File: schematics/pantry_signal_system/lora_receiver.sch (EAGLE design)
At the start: 6 parts, among them J1 JST-XH254-2P, U1 ESP32, U12 E220-900T22D, U2 SN74LVC2T45DCUR, U3 SN74LVC2T45DCUR

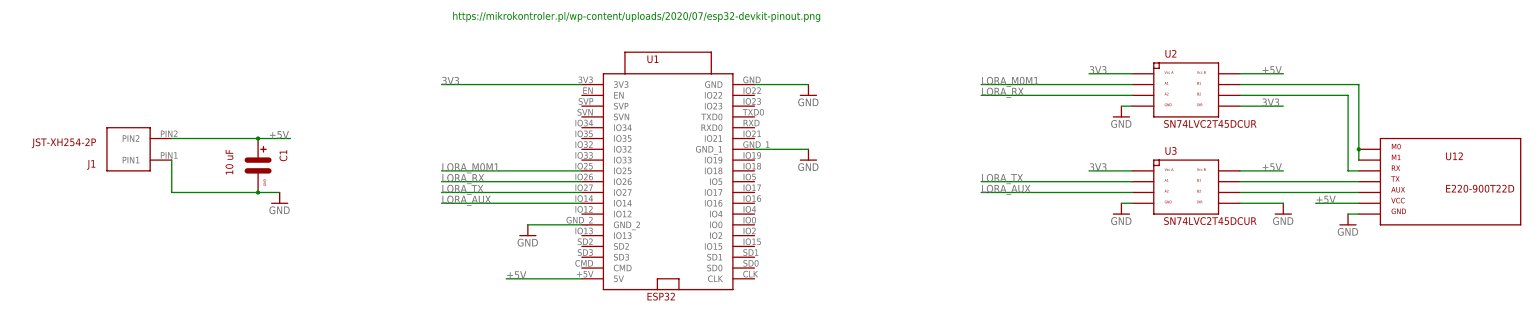
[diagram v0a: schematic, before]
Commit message: Changes in schematics, changes in source code. Current version works too, but I changed boards to fix some possible errors
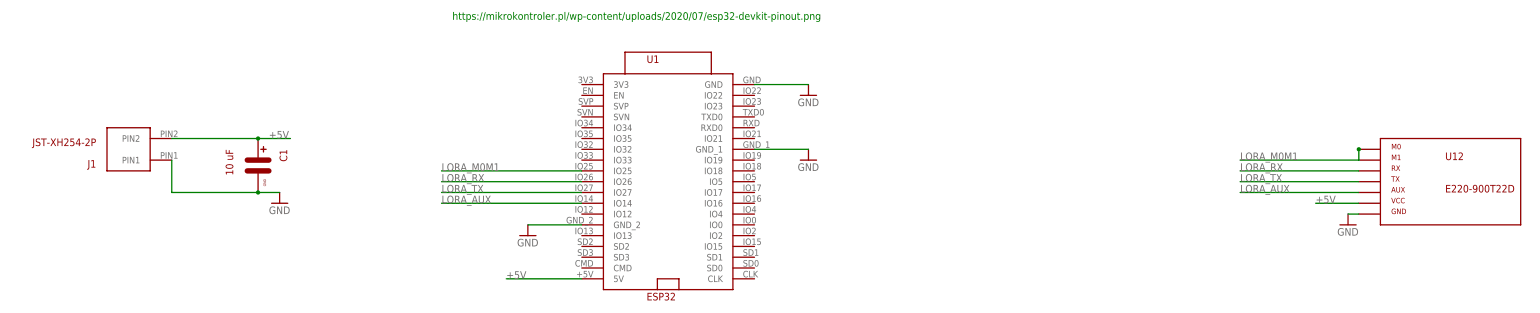
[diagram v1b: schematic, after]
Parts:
- removed U2, U3: SN74LVC2T45DCUR, my_devices:LEVEL_CONVERTER_2L
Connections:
- removed net 3V3: U1.3V3, U2.DIR, U2.VCCA, U3.VCCA
- removed net N$1: U12.TX, U3.B1
- removed net N$2: U12.RX, U2.B2
- removed net N$3: U12.AUX, U3.B2
- removed net N$9: U12.M0, U12.M1, U2.B1
- net +5V: no longer U2.VCCB, U3.VCCB
- net GND: no longer U2.GND, U3.DIR, U3.GND
- net LORA_AUX: now also U12.AUX; no longer U3.A2
- net LORA_M0M1: now also U12.M0, U12.M1; no longer U2.A1
- net LORA_RX: now also U12.RX; no longer U2.A2
- net LORA_TX: now also U12.TX; no longer U3.A1
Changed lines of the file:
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@@
 <part name="J1" library="my_devices" deviceset="JST-XH254-2P" device=""/>
 <part name="GND4" library="supply1" library_urn="urn:adsk.eagle:library:371" deviceset="GND" device=""/>
-<part name="U2" library="my_devices" deviceset="LEVEL_CONVERTER_2L" device="" value="SN74LVC2T45DCUR"/>
-<part name="U3" library="my_devices" deviceset="LEVEL_CONVERTER_2L" device="" value="SN74LVC2T45DCUR"/>
-<part name="GND5" library="supply1" library_urn="urn:adsk.eagle:library:371" deviceset="GND" device=""/>
-<part name="GND6" library="supply1" library_urn="urn:adsk.eagle:library:371" deviceset="GND" device=""/>
-<part name="GND7" library="supply1" library_urn="urn:adsk.eagle:library:371" deviceset="GND" device=""/>
 <part name="GND8" library="supply1" library_urn="urn:adsk.eagle:library:371" deviceset="GND" device=""/>
 <part name="C1" library="my_devices" deviceset="C" device="MINI-5X7" value="10 uF"/>
@@
 <attribute name="VALUE" x="-71.12" y="119.38" size="1.778" layer="96"/>
 </instance>
-<instance part="U2" gate="G$1" x="144.78" y="147.32" smashed="yes" grouprefs="LORA">
-<attribute name="NAME" x="139.7" y="156.21" size="1.778" layer="94"/>
-<attribute name="VALUE" x="139.446" y="139.7" size="1.778" layer="94"/>
-</instance>
-<instance part="U3" gate="G$1" x="144.78" y="124.46" smashed="yes" grouprefs="LORA">
-<attribute name="NAME" x="139.7" y="133.35" size="1.778" layer="94"/>
-<attribute name="VALUE" x="139.446" y="116.84" size="1.778" layer="94"/>
-</instance>
-<instance part="GND5" gate="1" x="129.54" y="142.24" smashed="yes" grouprefs="LORA">
-<attribute name="VALUE" x="127" y="139.7" size="1.778" layer="96"/>
-</instance>
-<instance part="GND6" gate="1" x="129.54" y="119.38" smashed="yes" grouprefs="LORA">
-<attribute name="VALUE" x="127" y="116.84" size="1.778" layer="96"/>
-</instance>
-<instance part="GND7" gate="1" x="167.64" y="119.38" smashed="yes" grouprefs="LORA">
-<attribute name="VALUE" x="165.1" y="116.84" size="1.778" layer="96"/>
-</instance>
 <instance part="GND8" gate="1" x="182.88" y="116.84" smashed="yes" grouprefs="LORA">
 <attribute name="VALUE" x="180.34" y="114.3" size="1.778" layer="96"/>
@@
 <pinref part="GND2" gate="1" pin="GND"/>
 <wire x1="43.18" y1="149.86" x2="55.88" y2="149.86" width="0.1524" layer="91" grouprefs="ESP32"/>
-</segment>
-<segment>
-<pinref part="GND5" gate="1" pin="GND"/>
-<pinref part="U2" gate="G$1" pin="GND"/>
-<wire x1="129.54" y1="144.78" x2="132.08" y2="144.78" width="0.1524" layer="91" grouprefs="LORA"/>
-</segment>
-<segment>
-<pinref part="GND6" gate="1" pin="GND"/>
-<pinref part="U3" gate="G$1" pin="GND"/>
-<wire x1="129.54" y1="121.92" x2="132.08" y2="121.92" width="0.1524" layer="91" grouprefs="LORA"/>
-</segment>
-<segment>
-<pinref part="U3" gate="G$1" pin="DIR"/>
-<pinref part="GND7" gate="1" pin="GND"/>
-<wire x1="157.48" y1="121.92" x2="167.64" y2="121.92" width="0.1524" layer="91" grouprefs="LORA"/>
 </segment>
 <segment>
@@
 </segment>
 <segment>
-<pinref part="U2" gate="G$1" pin="VCCB"/>
-<wire x1="157.48" y1="152.4" x2="167.64" y2="152.4" width="0.1524" layer="91" grouprefs="LORA"/>
-<label x="162.56" y="152.4" size="1.778" layer="95" grouprefs="LORA"/>
-</segment>
-<segment>
-<pinref part="U3" gate="G$1" pin="VCCB"/>
-<wire x1="157.48" y1="129.54" x2="167.64" y2="129.54" width="0.1524" layer="91" grouprefs="LORA"/>
-<label x="162.56" y="129.54" size="1.778" layer="95" grouprefs="LORA"/>
-</segment>
-<segment>
 <pinref part="U12" gate="G$1" pin="VCC"/>
 <wire x1="185.42" y1="121.92" x2="175.26" y2="121.92" width="0.1524" layer="91" grouprefs="LORA"/>
@@
 <net name="LORA_RX" class="0">
 <segment>
-<pinref part="U2" gate="G$1" pin="A2"/>
-<wire x1="132.08" y1="147.32" x2="96.52" y2="147.32" width="0.1524" layer="91" grouprefs="LORA"/>
-<label x="96.52" y="147.32" size="1.778" layer="95" grouprefs="LORA"/>
-</segment>
-<segment>
 <pinref part="U1" gate="G$1" pin="IO26"/>
 <wire x1="2.54" y1="127" x2="-30.48" y2="127" width="0.1524" layer="91" grouprefs="ESP32"/>
 <label x="-30.48" y="127" size="1.778" layer="95" grouprefs="ESP32"/>
 </segment>
+<segment>
+<pinref part="U12" gate="G$1" pin="RX"/>
+<wire x1="185.42" y1="129.54" x2="157.48" y2="129.54" width="0.1524" layer="91" grouprefs="LORA"/>
+<label x="157.48" y="129.54" size="1.778" layer="95"/>
+</segment>
 </net>
 <net name="LORA_TX" class="0">
-<segment>
-<pinref part="U3" gate="G$1" pin="A1"/>
-<wire x1="132.08" y1="127" x2="96.52" y2="127" width="0.1524" layer="91" grouprefs="LORA"/>
-<label x="96.52" y="127" size="1.778" layer="95" grouprefs="LORA"/>
-</segment>
 <segment>
 <pinref part="U1" gate="G$1" pin="IO27"/>
@@
 <label x="-30.48" y="124.46" size="1.778" layer="95" grouprefs="ESP32"/>
 </segment>
+<segment>
+<pinref part="U12" gate="G$1" pin="TX"/>
+<wire x1="157.48" y1="127" x2="185.42" y2="127" width="0.1524" layer="91" grouprefs="LORA"/>
+<label x="157.48" y="127" size="1.778" layer="95"/>
+</segment>
 </net>
 <net name="LORA_AUX" class="0">
-<segment>
-<pinref part="U3" gate="G$1" pin="A2"/>
-<wire x1="132.08" y1="124.46" x2="96.52" y2="124.46" width="0.1524" layer="91" grouprefs="LORA"/>
-<label x="96.52" y="124.46" size="1.778" layer="95" grouprefs="LORA"/>
-</segment>
 <segment>
 <pinref part="U1" gate="G$1" pin="IO14"/>
 <wire x1="2.54" y1="121.92" x2="-30.48" y2="121.92" width="0.1524" layer="91" grouprefs="ESP32"/>
 <label x="-30.48" y="121.92" size="1.778" layer="95" grouprefs="ESP32"/>
+</segment>
+<segment>
+<pinref part="U12" gate="G$1" pin="AUX"/>
+<wire x1="157.48" y1="124.46" x2="185.42" y2="124.46" width="0.1524" layer="91" grouprefs="LORA"/>
+<label x="157.48" y="124.46" size="1.778" layer="95"/>
 </segment>
 </net>
@@
 </segment>
 <segment>
-<pinref part="U2" gate="G$1" pin="A1"/>
-<wire x1="132.08" y1="149.86" x2="96.52" y2="149.86" width="0.1524" layer="91" grouprefs="LORA"/>
-<label x="96.52" y="149.86" size="1.778" layer="95" grouprefs="LORA"/>
+<pinref part="U12" gate="G$1" pin="M1"/>
+<pinref part="U12" gate="G$1" pin="M0"/>
+<wire x1="157.48" y1="132.08" x2="185.42" y2="132.08" width="0.1524" layer="91" grouprefs="LORA"/>
+<wire x1="185.42" y1="132.08" x2="185.42" y2="134.62" width="0.1524" layer="91" grouprefs="LORA"/>
+<junction x="185.42" y="134.62" grouprefs="LORA"/>
+<label x="157.48" y="132.08" size="1.778" layer="95"/>
 </segment>
 </net>
-<net name="N$9" class="0">
-<segment>
-<pinref part="U12" gate="G$1" pin="M1"/>
-<pinref part="U12" gate="G$1" pin="M0"/>
-<wire x1="185.42" y1="132.08" x2="185.42" y2="134.62" width="0.1524" layer="91" grouprefs="LORA"/>
-<pinref part="U2" gate="G$1" pin="B1"/>
-<wire x1="157.48" y1="149.86" x2="185.42" y2="149.86" width="0.1524" layer="91" grouprefs="LORA"/>
-<wire x1="185.42" y1="149.86" x2="185.42" y2="134.62" width="0.1524" layer="91" grouprefs="LORA"/>
-<junction x="185.42" y="134.62" grouprefs="LORA"/>
-</segment>
-</net>
-<net name="3V3" class="0">
-<segment>
-<pinref part="U1" gate="G$1" pin="3V3"/>
-<wire x1="2.54" y1="149.86" x2="-30.48" y2="149.86" width="0.1524" layer="91"/>
-<label x="-30.48" y="149.86" size="1.778" layer="95"/>
-</segment>
-<segment>
-<pinref part="U2" gate="G$1" pin="VCCA"/>
-<wire x1="132.08" y1="152.4" x2="121.92" y2="152.4" width="0.1524" layer="91" grouprefs="LORA"/>
-<label x="121.92" y="152.4" size="1.778" layer="95" grouprefs="LORA"/>
-</segment>
-<segment>
-<pinref part="U3" gate="G$1" pin="VCCA"/>
-<wire x1="132.08" y1="129.54" x2="121.92" y2="129.54" width="0.1524" layer="91" grouprefs="LORA"/>
-<label x="121.92" y="129.54" size="1.778" layer="95" grouprefs="LORA"/>
-</segment>
-<segment>
-<pinref part="U2" gate="G$1" pin="DIR"/>
-<wire x1="157.48" y1="144.78" x2="167.64" y2="144.78" width="0.1524" layer="91" grouprefs="LORA"/>
-<label x="162.56" y="144.78" size="1.778" layer="95" grouprefs="LORA"/>
-</segment>
-</net>
-<net name="N$2" class="0">
-<segment>
-<pinref part="U12" gate="G$1" pin="RX"/>
-<wire x1="185.42" y1="129.54" x2="182.88" y2="129.54" width="0.1524" layer="91" grouprefs="LORA"/>
-<wire x1="182.88" y1="129.54" x2="182.88" y2="147.32" width="0.1524" layer="91" grouprefs="LORA"/>
-<pinref part="U2" gate="G$1" pin="B2"/>
-<wire x1="182.88" y1="147.32" x2="157.48" y2="147.32" width="0.1524" layer="91" grouprefs="LORA"/>
-</segment>
-</net>
-<net name="N$1" class="0">
-<segment>
-<pinref part="U3" gate="G$1" pin="B1"/>
-<pinref part="U12" gate="G$1" pin="TX"/>
-<wire x1="157.48" y1="127" x2="185.42" y2="127" width="0.1524" layer="91" grouprefs="LORA"/>
-</segment>
-</net>
-<net name="N$3" class="0">
-<segment>
-<pinref part="U3" gate="G$1" pin="B2"/>
-<pinref part="U12" gate="G$1" pin="AUX"/>
-<wire x1="157.48" y1="124.46" x2="185.42" y2="124.46" width="0.1524" layer="91" grouprefs="LORA"/>
-</segment>
-</net>

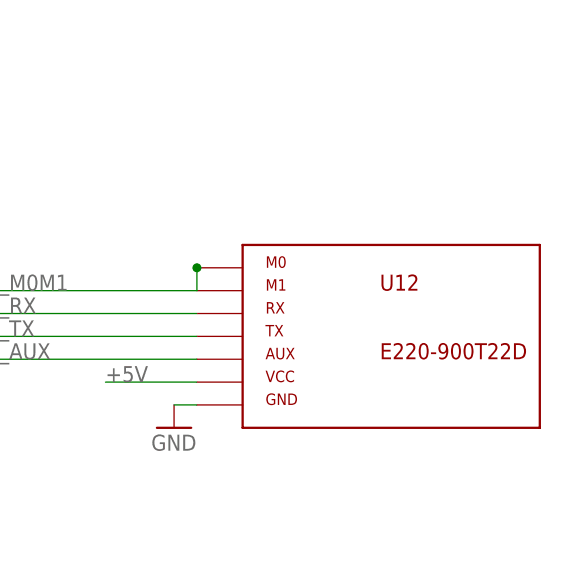
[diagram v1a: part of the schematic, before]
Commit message: Debugging logic module firmware, estabilishing LoRa connection....
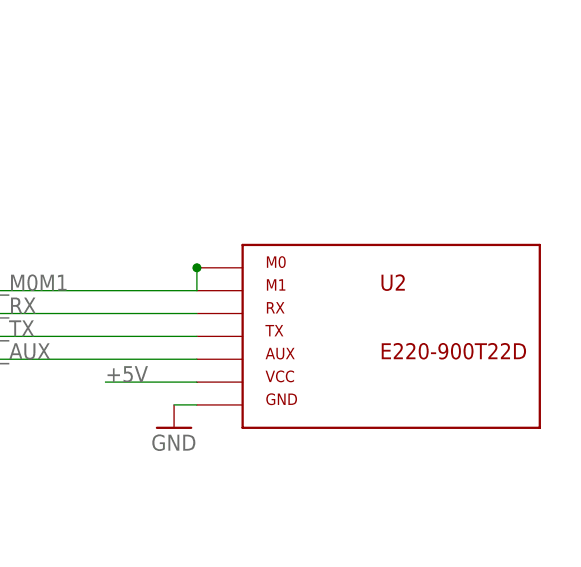
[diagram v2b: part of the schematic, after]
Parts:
- renumbered U12 to U2
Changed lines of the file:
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@@
 </groups>
 <parts>
-<part name="U12" library="my_devices" deviceset="LORA" device="" value="E220-900T22D"/>
+<part name="U2" library="my_devices" deviceset="LORA" device="" value="E220-900T22D"/>
 <part name="U1" library="my_devices" deviceset="ESP32" device=""/>
 <part name="GND1" library="supply1" library_urn="urn:adsk.eagle:library:371" deviceset="GND" device=""/>
@@
 </plain>
 <instances>
-<instance part="U12" gate="G$1" x="203.2" y="127" smashed="yes" grouprefs="LORA">
+<instance part="U2" gate="G$1" x="203.2" y="127" smashed="yes" grouprefs="LORA">
 <attribute name="NAME" x="205.74" y="132.08" size="1.778" layer="94"/>
 <attribute name="VALUE" x="205.74" y="124.46" size="1.778" layer="94"/>
@@
 <segment>
 <pinref part="GND8" gate="1" pin="GND"/>
-<pinref part="U12" gate="G$1" pin="GND"/>
+<pinref part="U2" gate="G$1" pin="GND"/>
 <wire x1="182.88" y1="119.38" x2="185.42" y2="119.38" width="0.1524" layer="91" grouprefs="LORA"/>
 </segment>
@@
 </segment>
 <segment>
-<pinref part="U12" gate="G$1" pin="VCC"/>
+<pinref part="U2" gate="G$1" pin="VCC"/>
 <wire x1="185.42" y1="121.92" x2="175.26" y2="121.92" width="0.1524" layer="91" grouprefs="LORA"/>
 <label x="175.26" y="121.92" size="1.778" layer="95" grouprefs="LORA"/>
@@
 </segment>
 <segment>
-<pinref part="U12" gate="G$1" pin="RX"/>
+<pinref part="U2" gate="G$1" pin="RX"/>
 <wire x1="185.42" y1="129.54" x2="157.48" y2="129.54" width="0.1524" layer="91" grouprefs="LORA"/>
 <label x="157.48" y="129.54" size="1.778" layer="95"/>
@@
 </segment>
 <segment>
-<pinref part="U12" gate="G$1" pin="TX"/>
+<pinref part="U2" gate="G$1" pin="TX"/>
 <wire x1="157.48" y1="127" x2="185.42" y2="127" width="0.1524" layer="91" grouprefs="LORA"/>
 <label x="157.48" y="127" size="1.778" layer="95"/>
@@
 </segment>
 <segment>
-<pinref part="U12" gate="G$1" pin="AUX"/>
+<pinref part="U2" gate="G$1" pin="AUX"/>
 <wire x1="157.48" y1="124.46" x2="185.42" y2="124.46" width="0.1524" layer="91" grouprefs="LORA"/>
 <label x="157.48" y="124.46" size="1.778" layer="95"/>
@@
 </segment>
 <segment>
-<pinref part="U12" gate="G$1" pin="M1"/>
-<pinref part="U12" gate="G$1" pin="M0"/>
+<pinref part="U2" gate="G$1" pin="M1"/>
+<pinref part="U2" gate="G$1" pin="M0"/>
 <wire x1="157.48" y1="132.08" x2="185.42" y2="132.08" width="0.1524" layer="91" grouprefs="LORA"/>
 <wire x1="185.42" y1="132.08" x2="185.42" y2="134.62" width="0.1524" layer="91" grouprefs="LORA"/>
